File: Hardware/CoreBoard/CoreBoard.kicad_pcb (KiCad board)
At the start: 2 copper layers, 135.1 x 84.3 mm, 93 parts, among them J1 RJ45_LED_Shielded, SW1 SW_Push, SW10 SW_Push, SW11 SW_Push, SW12 SW_Push, SW13 SW_Push, SW14 SW_Push, SW15 SW_Push, SW16 SW_SPDT, SW2 SW_Push, SW3 SW_Push, SW4 SW_Push, SW5 SW_Push, SW6 SW_Push, SW7 SW_Push, SW8 SW_Push, SW9 SW_Push, U1 Teensy4.1_DEV-16771, U3 SHHD003A0A, U4 74HC148, U5 74HC148, U6 74HC00, U7 OKI

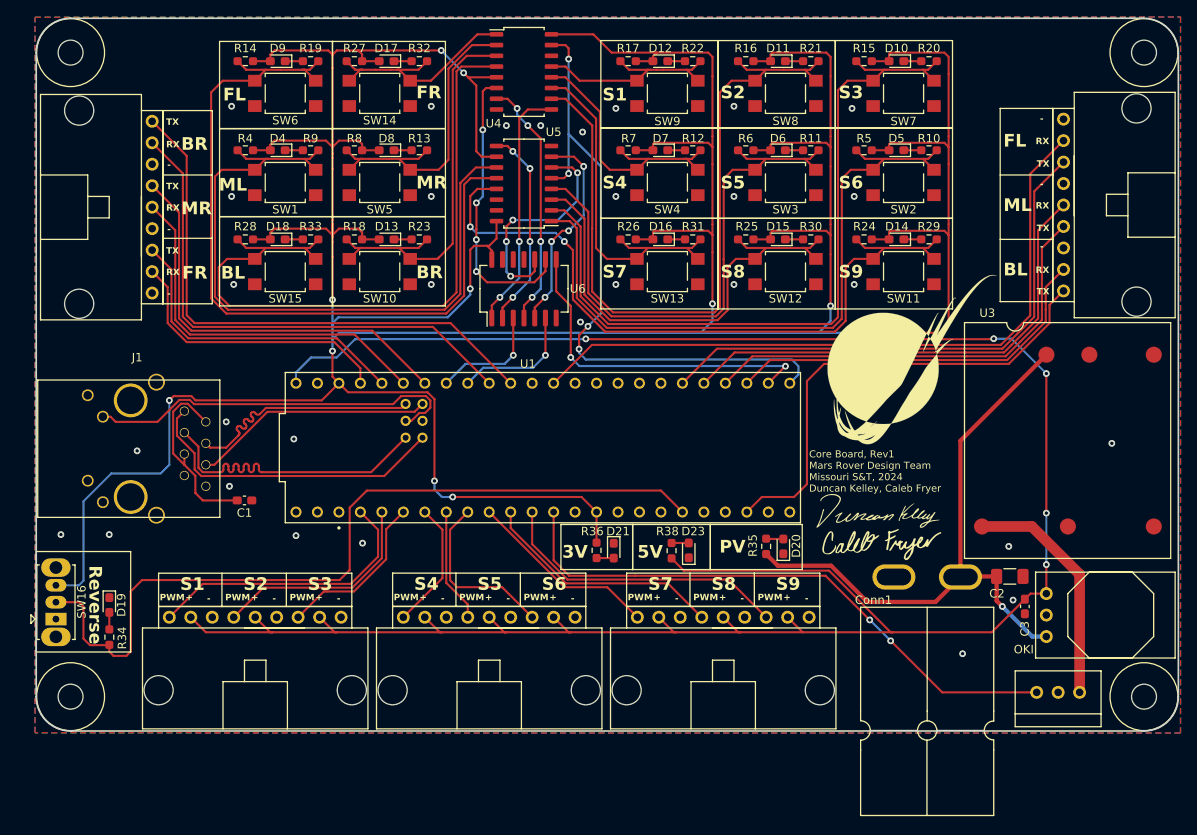
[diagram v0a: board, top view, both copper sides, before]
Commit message: made rev2 changes and cleaned up traces
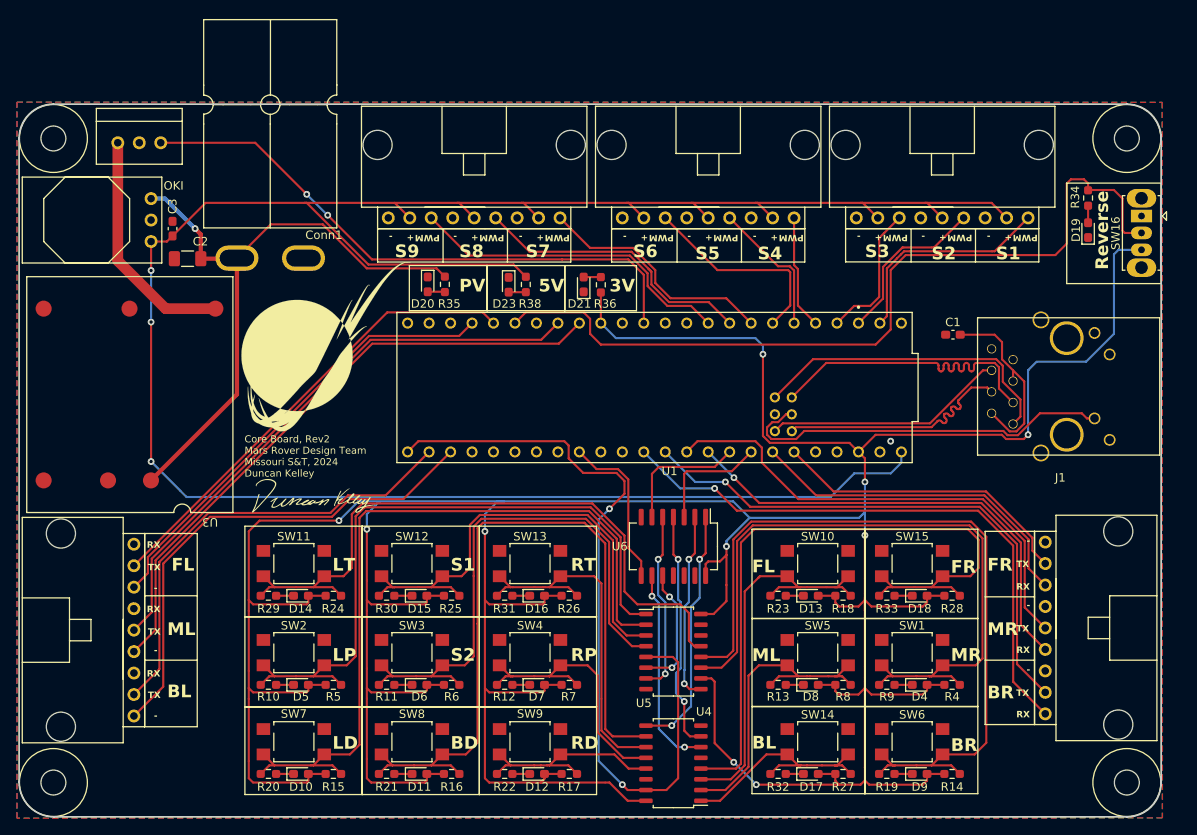
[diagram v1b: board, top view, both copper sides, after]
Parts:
- removed the G*** at (166.5, 93.8)
- moved REF** 155.3 mm to (68.8, 122.7), turned to 0 degrees
- moved REF** 151.9 mm to (195.8, 122.7), turned to 0 degrees
- moved REF** 145.0 mm to (68.8, 46.5), turned to 0 degrees
- moved REF** 141.3 mm to (195.8, 46.5), turned to 0 degrees
- moved SW16 137.0 mm to (197.6, 55.7), turned to -90 degrees
- moved J1 137.0 mm to (201.7, 75.7), turned to 90 degrees
- moved Conn7 131.1 mm to (76.5, 47.0), turned to 0 degrees
- moved Conn2 130.7 mm to (78.4, 114.8), turned to 90 degrees
- moved R34 126.9 mm to (191.2, 53.5), turned to 90 degrees
- moved D19 124.0 mm to (191.2, 57.3), turned to 90 degrees
- moved R14 118.8 mm to (175.2, 121.7), turned to 0 degrees
- moved U7 117.9 mm to (80.4, 53.6), turned to -90 degrees
- moved R20 115.0 mm to (94.3, 121.7), turned to 0 degrees
- moved D9 113.5 mm to (171.3, 121.7), turned to 0 degrees
- moved C3 110.3 mm to (82.9, 57.1), turned to 90 degrees
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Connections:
- Conn2 pad 1: GND -> BL_TX
- Conn2 pad 2: FL_RX -> BL_RX
- Conn2 pad 3: FL_TX -> GND
- Conn2 pad 4: GND -> ML_TX
- Conn2 pad 6: ML_TX -> GND
- Conn2 pad 7: GND -> FL_TX
- Conn2 pad 8: BL_RX -> FL_RX
- Conn2 pad 9: BL_TX -> GND
- U1 pad 0: unconnected-(U1-RX1-Pad0) -> ServoPWM1
- U1 pad 1: unconnected-(U1-TX1-Pad1) -> ServoPWM2
- U1 pad 10: ServoPWM9 -> unconnected-(U1-CS1-Pad10)
- U1 pad 14: FL_RX -> BR_TX
- U1 pad 15: unconnected-(U1-A1-Pad15) -> BR_RX
- U1 pad 16: BR_TX -> MR_RX
- U1 pad 17: BR_RX -> MR_TX
- U1 pad 2: ServoPWM1 -> ServoPWM3
- U1 pad 20: MR_TX -> FR_TX
- U1 pad 21: MR_RX -> FR_RX
- U1 pad 22: FR_TX -> unconnected-(U1-A8-Pad22)
- U1 pad 23: FR_RX -> unconnected-(U1-A9-Pad23)
- U1 pad 24: unconnected-(U1-A10-Pad24) -> ML_TX
- U1 pad 25: unconnected-(U1-A11-Pad25) -> ML_RX
- U1 pad 28: unconnected-(U1-RX7-Pad28) -> FL_RX
- U1 pad 29: unconnected-(U1-TX7-Pad29) -> FL_TX
- U1 pad 3: ServoPWM2 -> ServoPWM4
- U1 pad 30: BL_TX -> unconnected-(U1-CRX3-Pad30)
- U1 pad 34: Out2 -> BL_RX
- U1 pad 35: BL_RX -> BL_TX
- U1 pad 36: ML_TX -> unconnected-(U1-CS2-Pad36)
- U1 pad 37: ML_RX -> unconnected-(U1-CS3-Pad37)
- U1 pad 38: FL_TX -> unconnected-(U1-A14-Pad38)
- U1 pad 4: ServoPWM3 -> ServoPWM5
- U1 pad 41: unconnected-(U1-A17-Pad41) -> Out2
- U1 pad 5: ServoPWM4 -> ServoPWM6
- U1 pad 6: ServoPWM5 -> ServoPWM7
- U1 pad 7: ServoPWM6 -> ServoPWM8
- U1 pad 8: ServoPWM7 -> ServoPWM9
- U1 pad 9: ServoPWM8 -> unconnected-(U1-OUT1C-Pad9)
- U4 pad 5: +3V3 -> GND
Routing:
- net FL_RX: track 82.0 -> 55.5 mm
- net Out2: track 41.0 -> 19.2 mm, vias 2 -> 0
- net ML_TX: track 52.7 -> 73.6 mm
- net Out3: track 76.8 -> 92.6 mm, vias 4 -> 2
- net +3V3: track 529.5 -> 514.7 mm, vias 11 -> 10
- net MR_RX: track 44.6 -> 57.7 mm
- net Net-(U5-S2): track 26.9 -> 14.9 mm, vias 4 -> 2
- net ML_RX: track 57.4 -> 68.9 mm
- net FL_TX: track 64.6 -> 54.1 mm
- net Net-(U4-S2): track 34.1 -> 24.3 mm, vias 4 -> 2
- net BL_RX: track 45.4 -> 54.2 mm
- net ServoPWM1: track 33.9 -> 26.1 mm
- net ServoPWM2: track 25.9 -> 19.9 mm
- net MR_TX: track 49.3 -> 55.3 mm, vias 0 -> 1
- net ServoPWM7: track 22.7 -> 28.7 mm
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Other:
- outline, holes or cut-outs redrawn
- board text added: "BD"
- board text added: "Core Board, Rev2 Mars Rover Design Team Missouri S&T, 2024 Duncan Kelley"
- board text added: "LD"
- board text added: "LP"
- board text added: "LT"
- board text added: "RD"
- board text added: "RP"
- board text added: "RT"
- board text removed: "Core Board, Rev1 Mars Rover Design Team Missouri S&T, 2024 Duncan Kelley, Caleb Fryer"

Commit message: re-upload, didn't save last time
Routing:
- net +5V: track 275.0 -> 274.3 mm
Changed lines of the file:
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@@
     (effects (font (size 0.762 0.762) (thickness 0.1905) bold) (justify left bottom))
   )
-  (gr_text "PWM" (at 185.293 57.785 180) (layer "F.SilkS")
-    (effects (font (size 0.762 0.762) (thickness 0.1905) bold) (justify left bottom))
-  )
-  (gr_text "PWM" (at 122.174 57.7977 180) (layer "F.SilkS")
+  (gr_text "PWM" (at 112.141 58.547) (layer "F.SilkS")
+    (effects (font (size 0.762 0.762) (thickness 0.1905) bold) (justify left bottom))
+  )
+  (gr_text "PWM" (at 175.26 58.5343) (layer "F.SilkS")
     (effects (font (size 0.762 0.762) (thickness 0.1905) bold) (justify left bottom))
   )
@@
     (effects (font (size 0.762 0.762) (thickness 0.1905) bold) (justify left bottom))
   )
-  (gr_text "PWM" (at 169.926 57.785 180) (layer "F.SilkS")
+  (gr_text "PWM" (at 127.254 58.547) (layer "F.SilkS")
     (effects (font (size 0.762 0.762) (thickness 0.1905) bold) (justify left bottom))
   )
@@
     (effects (font (size 0.762 0.762) (thickness 0.1905) bold) (justify left bottom))
   )
-  (gr_text "PWM" (at 177.546 57.785 180) (layer "F.SilkS")
+  (gr_text "PWM" (at 119.888 58.547) (layer "F.SilkS")
     (effects (font (size 0.762 0.762) (thickness 0.1905) bold) (justify left bottom))
   )
@@
     (effects (font (size 0.762 0.762) (thickness 0.1905) bold) (justify left bottom))
   )
-  (gr_text "+" (at 139.192 57.7977 180) (layer "F.SilkS")
+  (gr_text "+" (at 158.242 58.5343) (layer "F.SilkS")
     (effects (font (size 0.762 0.762) (thickness 0.1905) bold) (justify left bottom))
   )
@@
     (effects (font (size 1.5 1.5) (thickness 0.3) bold) (justify left bottom))
   )
-  (gr_text "PWM" (at 149.86 57.7977 180) (layer "F.SilkS")
+  (gr_text "PWM" (at 147.574 58.5343) (layer "F.SilkS")
     (effects (font (size 0.762 0.762) (thickness 0.1905) bold) (justify left bottom))
   )
@@
     (effects (font (size 1.5 1.5) (thickness 0.3) bold) (justify left bottom))
   )
-  (gr_text "PWM" (at 157.607 57.7977 180) (layer "F.SilkS")
+  (gr_text "PWM" (at 139.827 58.5343) (layer "F.SilkS")
     (effects (font (size 0.762 0.762) (thickness 0.1905) bold) (justify left bottom))
   )
@@
     (effects (font (size 0.762 0.762) (thickness 0.1905) bold) (justify left bottom))
   )
-  (gr_text "PWM" (at 129.921 57.7977 180) (layer "F.SilkS")
-    (effects (font (size 0.762 0.762) (thickness 0.1905) bold) (justify left bottom))
-  )
-  (gr_text "PWM" (at 142.24 57.7977 180) (layer "F.SilkS")
+  (gr_text "PWM" (at 167.513 58.5343) (layer "F.SilkS")
+    (effects (font (size 0.762 0.762) (thickness 0.1905) bold) (justify left bottom))
+  )
+  (gr_text "PWM" (at 154.94 58.5343) (layer "F.SilkS")
     (effects (font (size 0.762 0.762) (thickness 0.1905) bold) (justify left bottom))
   )
@@
     (effects (font (size 1.5 1.5) (thickness 0.3) bold) (justify left bottom))
   )
-  (gr_text "PWM" (at 114.554 57.7977 180) (layer "F.SilkS")
+  (gr_text "PWM" (at 182.626 58.5343) (layer "F.SilkS")
     (effects (font (size 0.762 0.762) (thickness 0.1905) bold) (justify left bottom))
   )
@@
   (gr_text "RD" (at 130.048 118.872) (layer "F.SilkS")
     (effects (font (size 1.5 1.5) (thickness 0.3) bold) (justify left bottom))
+  )
+  (gr_text "+" (at 139.192 57.658 180) (layer "F.SilkS")
+    (effects (font (size 0.762 0.762) (thickness 0.1905) bold) (justify left bottom))
   )
   (gr_text "S4" (at 152.146 60.96) (layer "F.SilkS")
@@
   (segment (start 80.391 62.103) (end 80.391 68.199) (width 0.254) (layer "B.Cu") (net 4))
   (segment (start 84.582 88.9) (end 83.82 88.138) (width 0.25) (layer "B.Cu") (net 4))
-  (segment (start 169.164 83.566) (end 169.164 84.836) (width 0.25) (layer "B.Cu") (net 4))
-  (segment (start 169.164 84.836) (end 167.894 86.106) (width 0.25) (layer "B.Cu") (net 4))
+  (segment (start 169.164 83.566) (end 166.624 86.106) (width 0.25) (layer "B.Cu") (net 4))
   (segment (start 80.391 84.709) (end 83.82 88.138) (width 0.254) (layer "B.Cu") (net 4))
   (segment (start 160.782 88.9) (end 84.582 88.9) (width 0.25) (layer "B.Cu") (net 4))
+  (segment (start 166.624 86.106) (end 163.576 86.106) (width 0.25) (layer "B.Cu") (net 4))
   (segment (start 163.576 86.106) (end 160.782 88.9) (width 0.25) (layer "B.Cu") (net 4))
-  (segment (start 167.894 86.106) (end 163.576 86.106) (width 0.25) (layer "B.Cu") (net 4))
   (segment (start 120.904 68.326) (end 119.634 67.056) (width 0.254) (layer "F.Cu") (net 5))
   (segment (start 119.634 67.056) (end 108.331 67.056) (width 0.254) (layer "F.Cu") (net 5))
@@
   (segment (start 184.204 97.336) (end 184.204 93.914052) (width 0.254) (layer "F.Cu") (net 69))
   (segment (start 184.204 93.914052) (end 178.989948 88.7) (width 0.254) (layer "F.Cu") (net 69))
+  (segment (start 129.794 82.931) (end 129.159 82.296) (width 0.254) (layer "F.Cu") (net 70))
+  (segment (start 129.159 82.296) (end 112.014 82.296) (width 0.254) (layer "F.Cu") (net 70))
+  (segment (start 141.351 123.571) (end 138.9392 123.571) (width 0.254) (layer "F.Cu") (net 70))
+  (segment (start 129.794 84.328) (end 129.794 82.931) (width 0.254) (layer "F.Cu") (net 70))
+  (segment (start 142.748 122.174) (end 141.351 123.571) (width 0.254) (layer "F.Cu") (net 70))
+  (segment (start 112.014 82.296) (end 110.744 83.566) (width 0.254) (layer "F.Cu") (net 70))
+  (segment (start 138.9392 107.823) (end 142.113 107.823) (width 0.254) (layer "F.Cu") (net 70))
   (segment (start 134.62 90.297) (end 136.398 88.519) (width 0.254) (layer "F.Cu") (net 70))
-  (segment (start 141.351 123.571) (end 138.9392 123.571) (width 0.254) (layer "F.Cu") (net 70))
-  (segment (start 112.014 82.296) (end 110.744 83.566) (width 0.254) (layer "F.Cu") (net 70))
-  (segment (start 142.748 122.174) (end 141.351 123.571) (width 0.254) (layer "F.Cu") (net 70))
-  (segment (start 138.9392 107.823) (end 142.113 107.823) (width 0.254) (layer "F.Cu") (net 70))
-  (segment (start 129.286 82.296) (end 112.014 82.296) (width 0.254) (layer "F.Cu") (net 70))
-  (segment (start 129.794 82.804) (end 129.286 82.296) (width 0.254) (layer "F.Cu") (net 70))
+  (segment (start 136.398 88.519) (end 136.398 87.002052) (width 0.254) (layer "F.Cu") (net 70))
   (segment (start 142.748 108.458) (end 142.748 115.316) (width 0.254) (layer "F.Cu") (net 70))
+  (segment (start 135.447948 86.052) (end 131.518 86.052) (width 0.254) (layer "F.Cu") (net 70))
   (segment (start 142.748 115.316) (end 142.748 122.174) (width 0.254) (layer "F.Cu") (net 70))
+  (segment (start 136.398 87.002052) (end 135.447948 86.052) (width 0.254) (layer "F.Cu") (net 70))
+  (segment (start 142.113 107.823) (end 142.748 108.458) (width 0.254) (layer "F.Cu") (net 70))
+  (segment (start 136.779 123.571) (end 138.9392 123.571) (width 0.254) (layer "F.Cu") (net 70))
   (segment (start 131.518 86.052) (end 129.794 84.328) (width 0.254) (layer "F.Cu") (net 70))
-  (segment (start 135.447948 86.052) (end 131.518 86.052) (width 0.254) (layer "F.Cu") (net 70))
-  (segment (start 142.113 107.823) (end 142.748 108.458) (width 0.254) (layer "F.Cu") (net 70))
-  (segment (start 129.794 84.328) (end 129.794 82.804) (width 0.254) (layer "F.Cu") (net 70))
-  (segment (start 136.779 123.571) (end 138.9392 123.571) (width 0.254) (layer "F.Cu") (net 70))
-  (segment (start 136.398 88.519) (end 136.398 87.002052) (width 0.254) (layer "F.Cu") (net 70))
-  (segment (start 136.398 87.002052) (end 135.447948 86.052) (width 0.254) (layer "F.Cu") (net 70))
   (segment (start 136.144 122.936) (end 136.779 123.571) (width 0.254) (layer "F.Cu") (net 70))
   (via (at 136.144 122.936) (size 0.8) (drill 0.4) (layers "F.Cu" "B.Cu") (net 70))
@@
     (connect_pads yes (clearance 0.127))
     (min_thickness 0.254) (filled_areas_thickness no)
-    (fill (thermal_gap 0.508) (thermal_bridge_width 0.508))
+    (fill yes (thermal_gap 0.508) (thermal_bridge_width 0.508))
     (polygon
       (pts

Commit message: changed according to discord message
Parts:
- U3: footprint MRDT_Devices:SHHD003A0A-SRZ -> MRDT_Devices:SHHD003A0A41Z_Through_Hole
- moved C2 10.3 mm to (94.2, 64.5), turned to 0 degrees
- moved C3 1.55 mm to (84.3, 57.8)
- moved G*** 0.76 mm to (99.6, 89.5)
- moved G*** 0.76 mm to (101.1, 71.9)
- moved Conn3 0.25 mm to (186.2, 94.0)
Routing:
- net PV: track 74.1 -> 81.5 mm, vias 1 -> 0
- net FL_RX: track 55.5 -> 61.4 mm
- net FL_TX: track 54.1 -> 59.2 mm
- net ML_RX: track 68.9 -> 74.0 mm
- net ML_TX: track 73.6 -> 78.7 mm
- net +3V3: track 514.7 -> 517.1 mm, vias 10 -> 9
- net MR_RX: track 57.7 -> 56.7 mm
- net BR_TX: track 69.8 -> 68.8 mm
- net FR_RX: track 36.1 -> 35.1 mm
- net BR_RX: track 65.1 -> 64.1 mm
- net MR_TX: track 55.3 -> 54.3 mm
- net FR_TX: track 40.8 -> 39.8 mm
- net Net-(U3-Vout+): track 27.9 -> 27.3 mm
- net +5V: track 274.3 -> 274.7 mm, vias 3 -> 0
- net NeoPixels: vias 2 -> 1
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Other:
- board text removed: "S3"
- board text removed: "S4"
- board text removed: "S5"
- board text removed: "S6"
- board text removed: "S7"
- board text removed: "S8"
- board text removed: "S9"

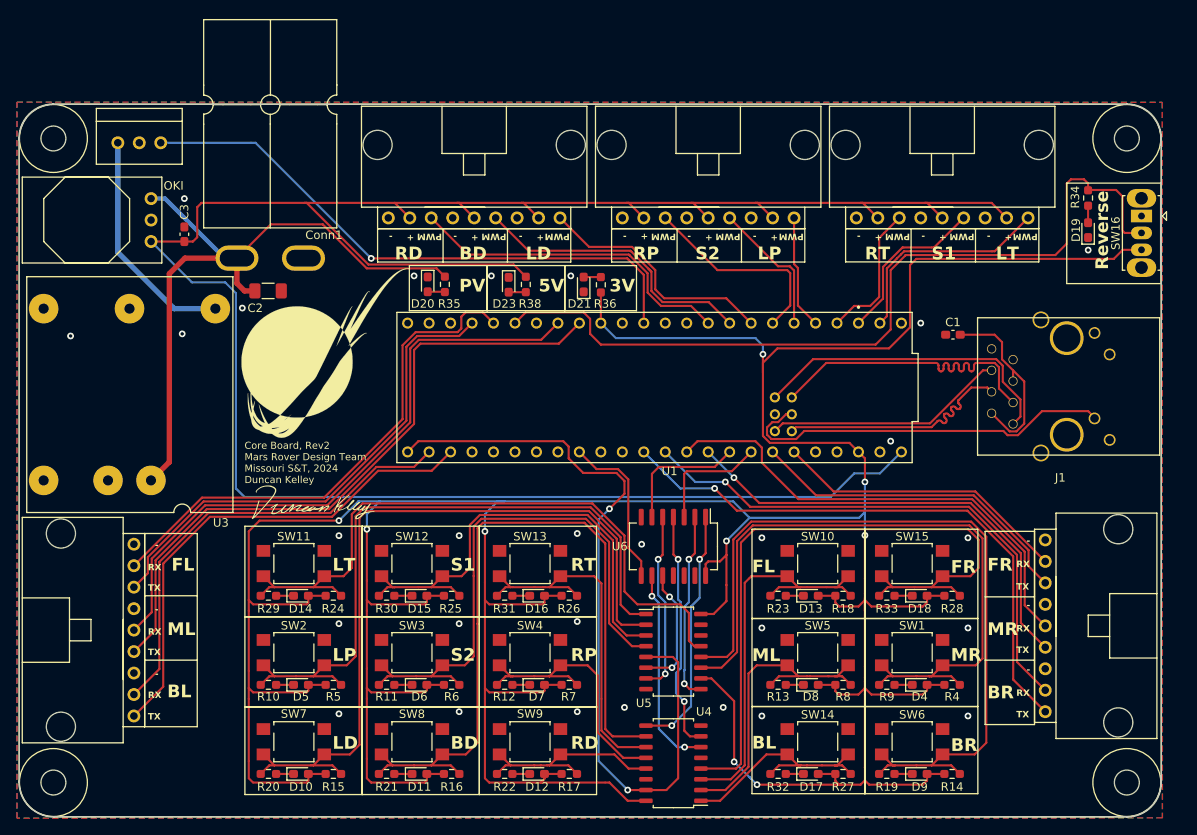
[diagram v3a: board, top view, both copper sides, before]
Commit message: flipped pwm labels and organized servos by right/left
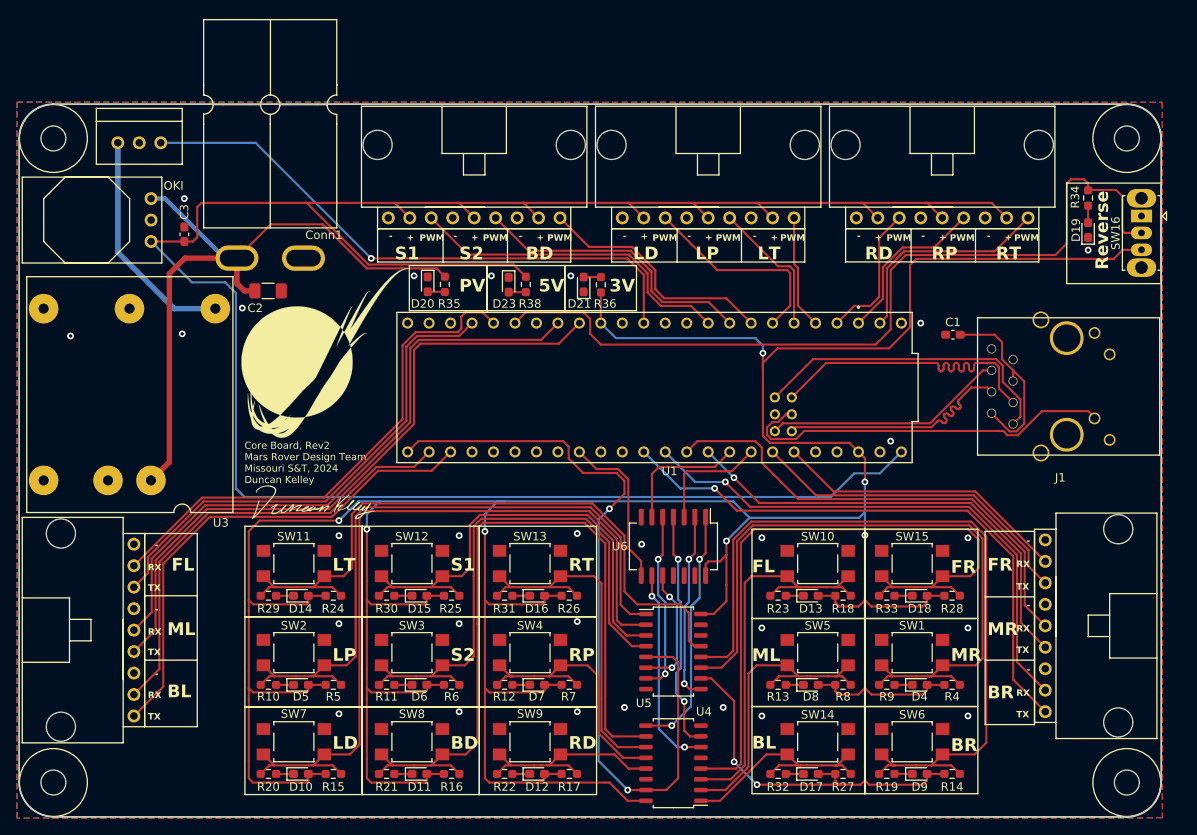
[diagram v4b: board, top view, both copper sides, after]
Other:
- board text added: "S3"
- board text added: "S4"
- board text added: "S5"
- board text added: "S6"
- board text added: "S7"
- board text added: "S8"
- board text added: "S9"
